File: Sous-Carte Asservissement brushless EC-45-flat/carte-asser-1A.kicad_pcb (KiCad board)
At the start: 2 copper layers, 60 x 62.5 mm, 57 parts, among them K1 Maxon-200142, K2 Maxon-200142, P1 swdio, P2 CAN bus, P3 usb, P4 serial bus, P5 5V, P6 8..24V, P7 encoder 1, P8 encoder 2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

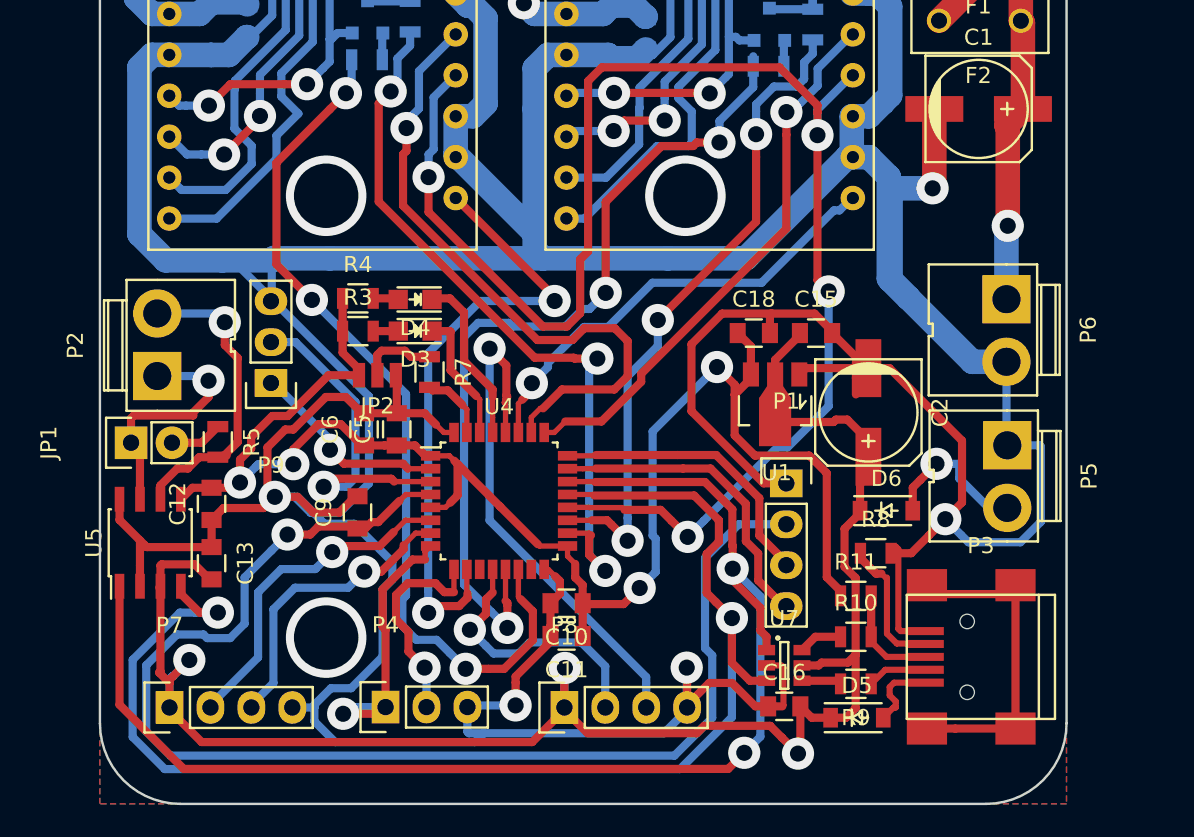
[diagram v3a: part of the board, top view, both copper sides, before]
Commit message: added B-plugs for power
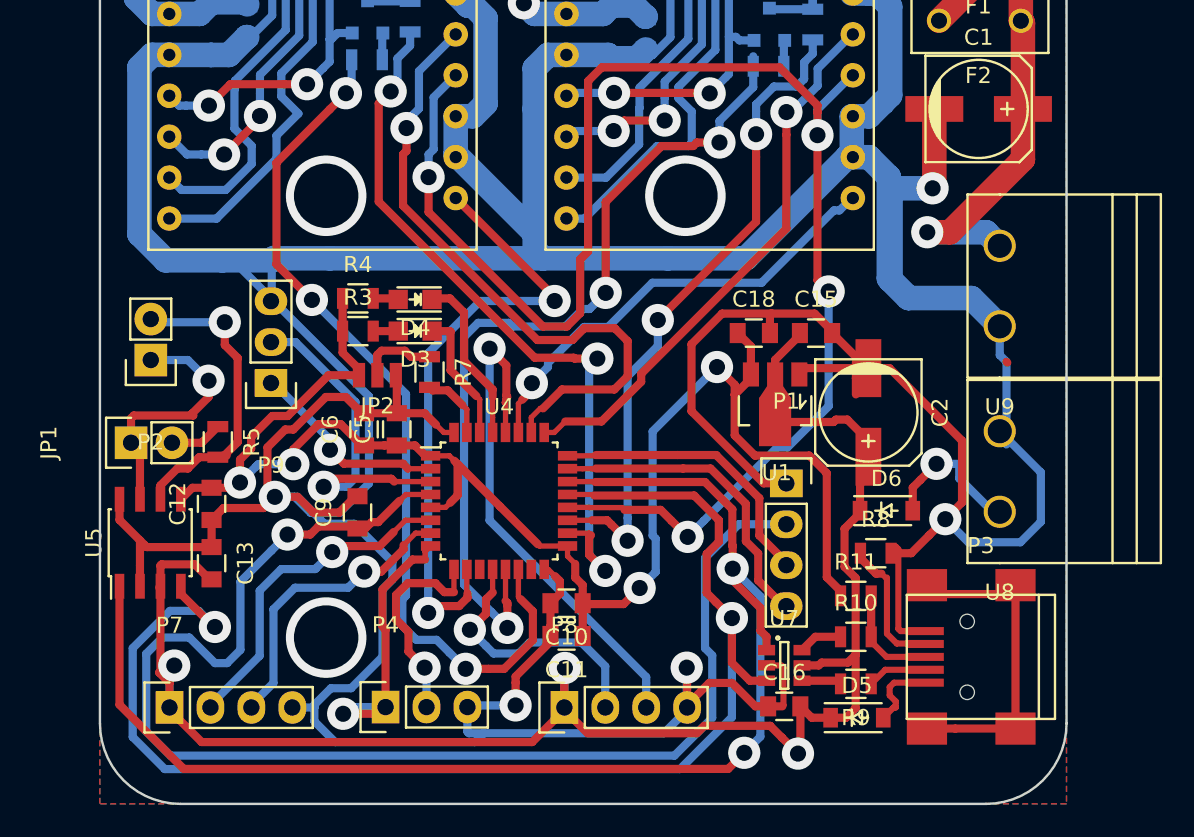
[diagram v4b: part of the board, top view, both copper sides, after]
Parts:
- removed P5: 5V, Connect:JWT_Vertical_A3963-RM3.96mm-2
- removed P6: 8..24V, Connect:JWT_Vertical_A3963-RM3.96mm-2
- added U8: 5v input, lib:B-plug-5mm, F.Cu at (169.3, 107.1)
- added U9: 12v input, lib:B-plug-5mm, F.Cu at (169.3, 95.6)
- P2: footprint Connect:JWT_Vertical_A3963-RM3.96mm-2 -> Pin_Headers:Pin_Header_Straight_1x02
- moved P2 1.07 mm to (116.6, 100.2), turned to 180 degrees
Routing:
- net +24V: track 22.8 -> 26.3 mm
- net /uC-part/nrst: track 81.3 -> 83.7 mm
- net +5V: track 109.4 -> 107.9 mm
- net Net-(JP1-Pad1): track 15.6 -> 16.9 mm
- net /uC-part/can_rx: track 82.5 -> 83.4 mm
- net GND: track 424.8 -> 425.5 mm
- net Net-(P2-Pad2): track 19.3 -> 20.0 mm

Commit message: added a nice logo :)
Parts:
- added G***: LOGO, logo:phelma-logo, B.Cu at (166.7, 68.9)
- added G***: LOGO, logo:phelma-logo-exp, B.Cu at (140.8, 108.2)
- moved F2 1.15 mm to (168.2, 78.0)
- moved F1 1.00 mm to (168.3, 73.9)
- moved P2 0.98 mm to (115.8, 99.7)
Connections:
- U4 pad 18: /uC-part/pwm2_pos -> /uC-part/pwm1_pos
- U4 pad 19: /uC-part/pwm1_pos -> /uC-part/pwm2_pos
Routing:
- net /uC-part/pwm1_pos: track 40.9 -> 53.1 mm
- net GND: track 425.5 -> 437.6 mm
- net /uC-part/pwm2_pos: track 46.9 -> 56.7 mm
- net Net-(D6-Pad2): track 9.82 -> 18.2 mm
- net /uC-part/gpio_direction2: track 40.2 -> 47.7 mm
- net /encoder-part/encoder2_2: track 32.1 -> 37.7 mm
- net Net-(JP1-Pad1): track 16.9 -> 12.0 mm, vias 1 -> 0
- net +3V3: track 100.2 -> 104.2 mm
- net Net-(P2-Pad2): track 20.0 -> 23.7 mm
- net /uC-part/gpio_direction1: track 34.5 -> 36.8 mm
- net /uC-part/pwm1_neg: track 53.4 -> 55.7 mm
- net /uC-part/gpio_enable: track 96.0 -> 94.1 mm
- net /uC-part/gpio_ready2: track 38.9 -> 40.2 mm
- net /uC-part/nrst: track 83.7 -> 84.9 mm
- net /brushless-part/power2: track 79.7 -> 78.5 mm
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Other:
- rule trace_min: 0.2 -> 0.007874
- rule via_min_size: 0.4 -> 0.015748
- board text added: "5v a b gnd"
- board text added: "5v gnd"
- board text added: "Logo : Antonin Macquart"
- board text added: "Lucien Dos Santos Farret RobotroniK Phelma 2016"
- board text added: "Motor A"
- board text added: "Motor B"
- board text added: "canl canh"
- board text added: "gnd 24v"
- board text added: "gnd scl sda"
- board text added: "rx tx gnd"

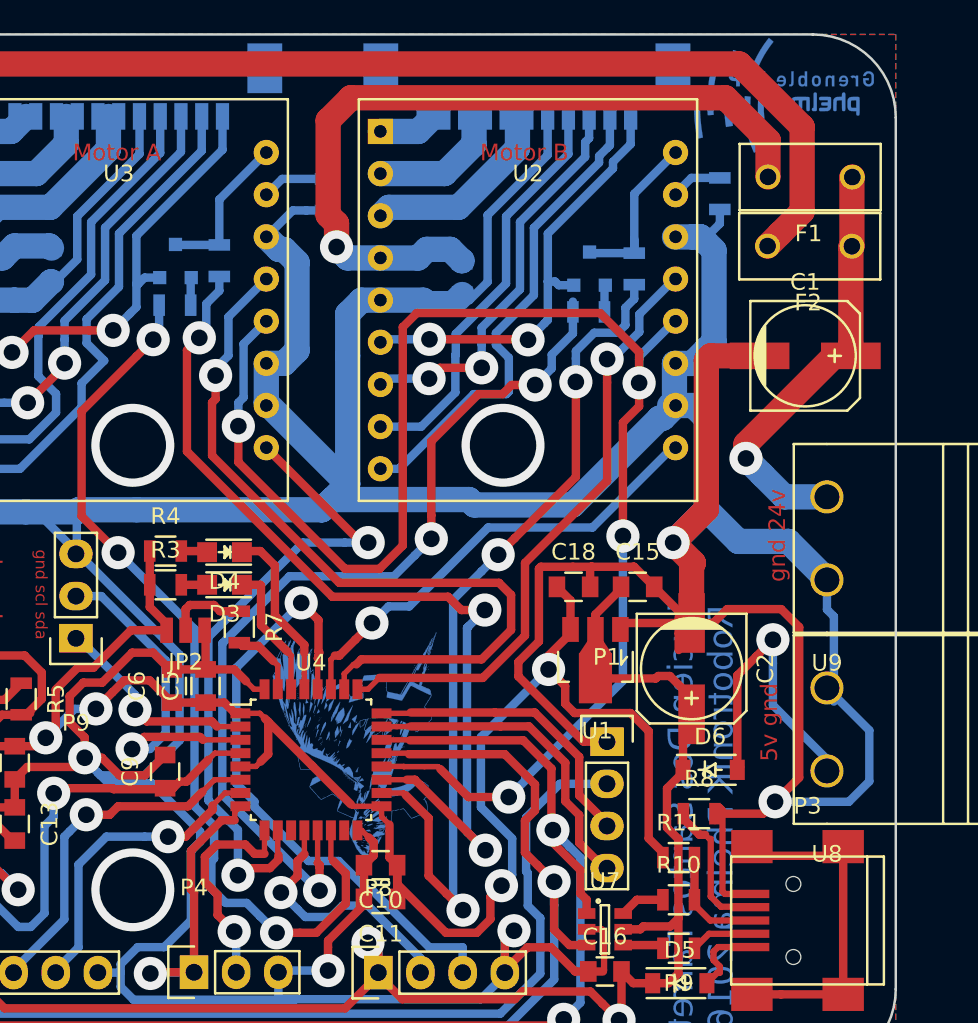
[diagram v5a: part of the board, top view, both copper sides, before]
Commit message: asser 1A : BOM + ready for pisa !
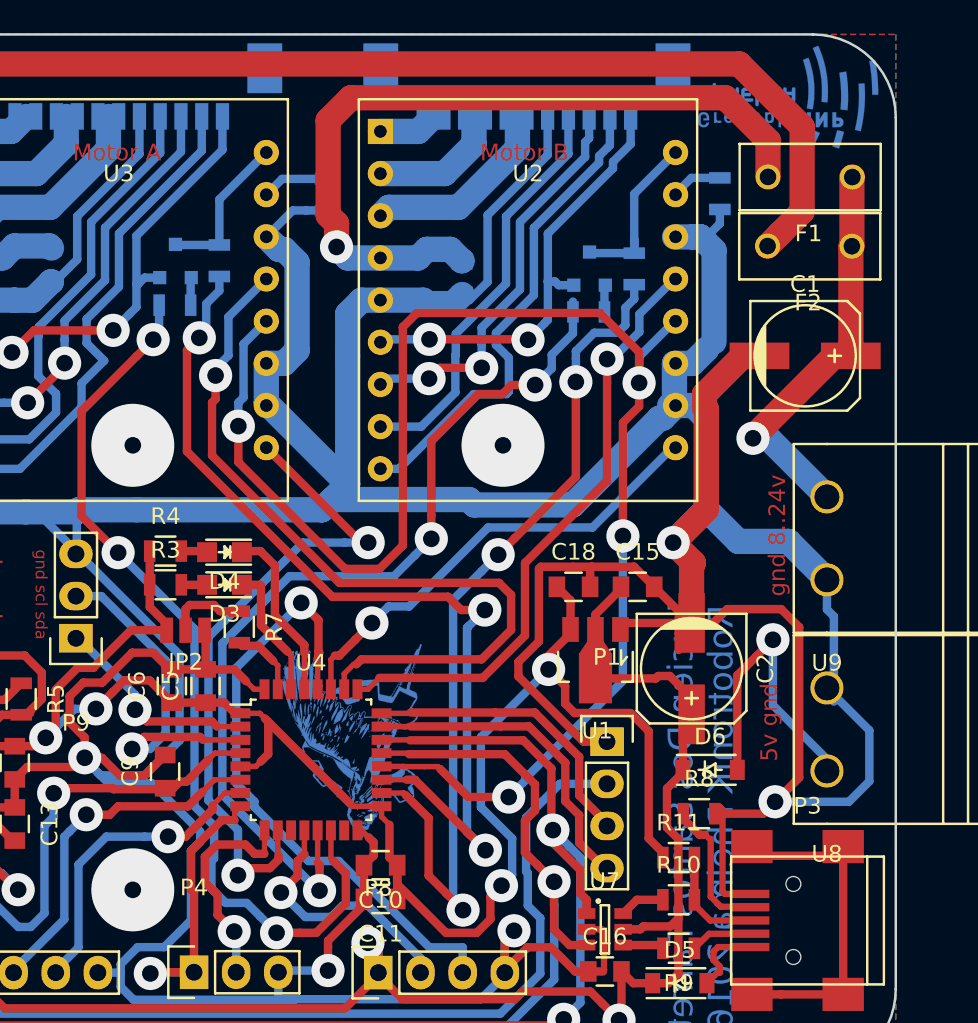
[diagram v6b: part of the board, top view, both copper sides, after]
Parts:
- removed the G*** at (140.8, 108.2)
- added G***: LOGO, logo:phelma-logo-exp3, B.Cu at (140.6, 107.9)
- C1: footprint Capacitors_SMD:c_elec_6.3x4.5 -> Capacitors_SMD:c_elec_6.3x7.7
- C2: footprint Capacitors_SMD:c_elec_6.3x4.5 -> Capacitors_SMD:c_elec_6.3x5.8
- moved G*** 0.59 mm to (166.9, 69.4), turned to 0 degrees
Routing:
- net GND: track 437.6 -> 434.9 mm
- net +24V: track 26.7 -> 25.4 mm
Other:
- board text added: "gnd 8..24v"
- board text removed: "gnd 24v"

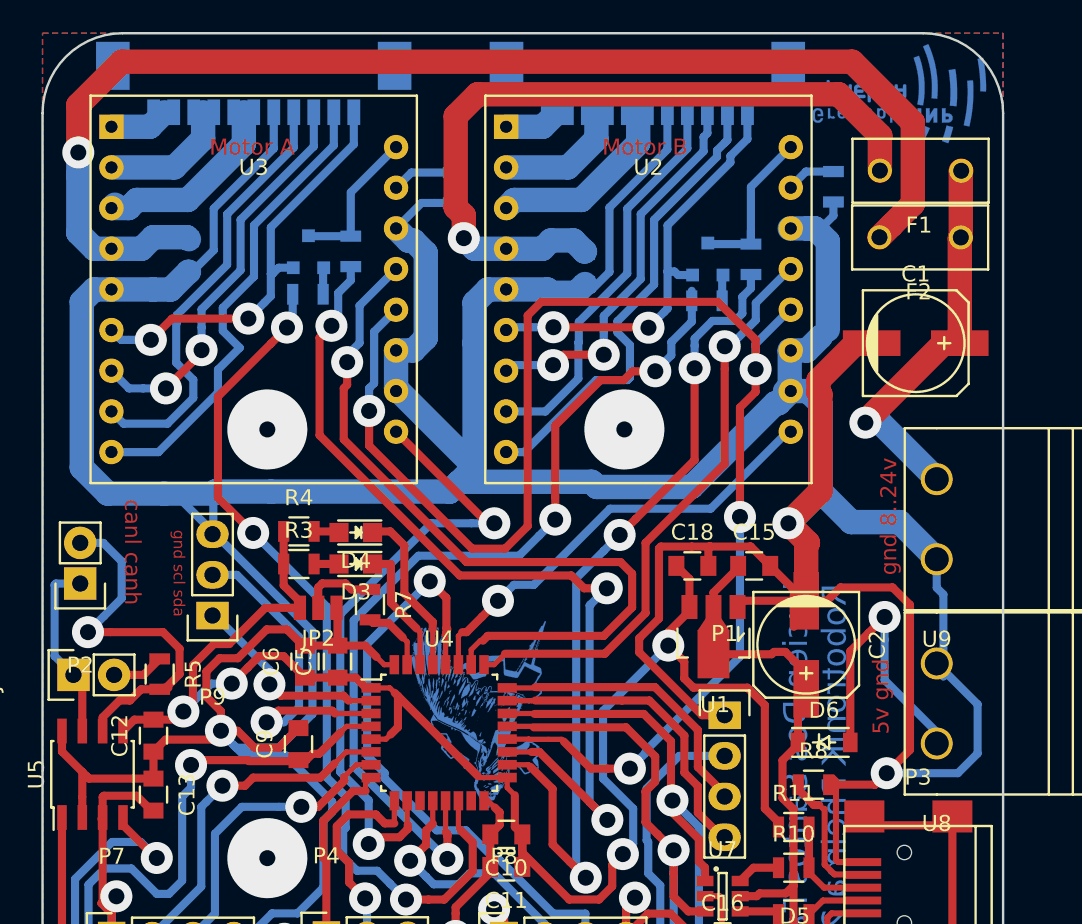
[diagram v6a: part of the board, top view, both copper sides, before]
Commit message: asser 1A : corrected zif sockets
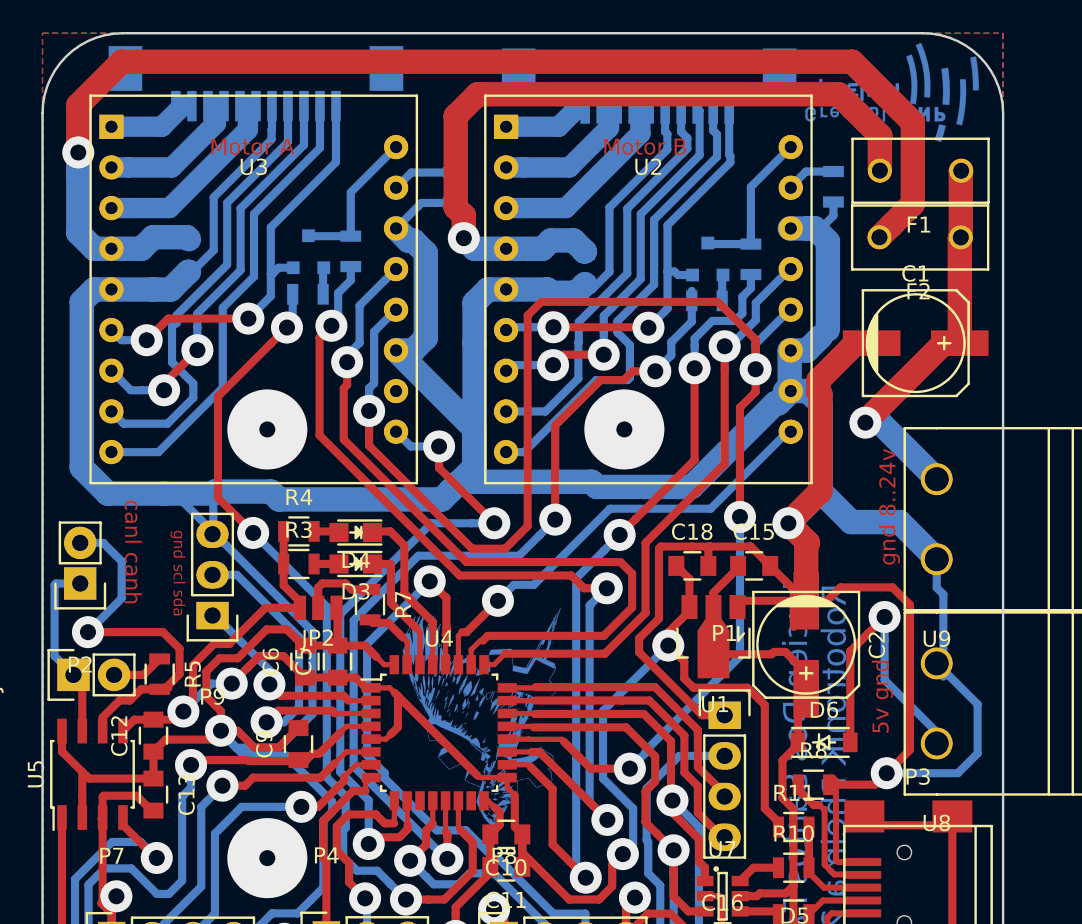
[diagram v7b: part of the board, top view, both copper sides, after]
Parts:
- removed the G*** at (140.6, 107.9)
- added G***: LOGO, logo:phelma-logo-exp, B.Cu at (140.8, 108.1)
- K1, K2: footprint Connectors_Molex:Molex_PicoBlade_53261-1171 -> de24-2:Molex-52207-0433
- moved K1 2.67 mm to (151.3, 70.0)
- moved K2 2.52 mm to (126.8, 69.8)
- moved G*** 0.46 mm to (166.5, 69.4)
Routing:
- net /uC-part/gpio_ready2: track 40.2 -> 41.4 mm, vias 2 -> 3
- net /brushless-part/W1_1: track 4.81 -> 5.90 mm
- net GND: track 434.9 -> 435.9 mm
- net /brushless-part/W2_1: track 4.94 -> 5.91 mm
- net Net-(K2-Pad10): track 29.6 -> 28.7 mm
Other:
- net class Default: clearance 0.3302 -> 0.254
- net class fat: clearance 0.508 -> 0.254; trace_width 1.524 -> 1.27
- rule trace_clearance: 0.3302 -> 0.254

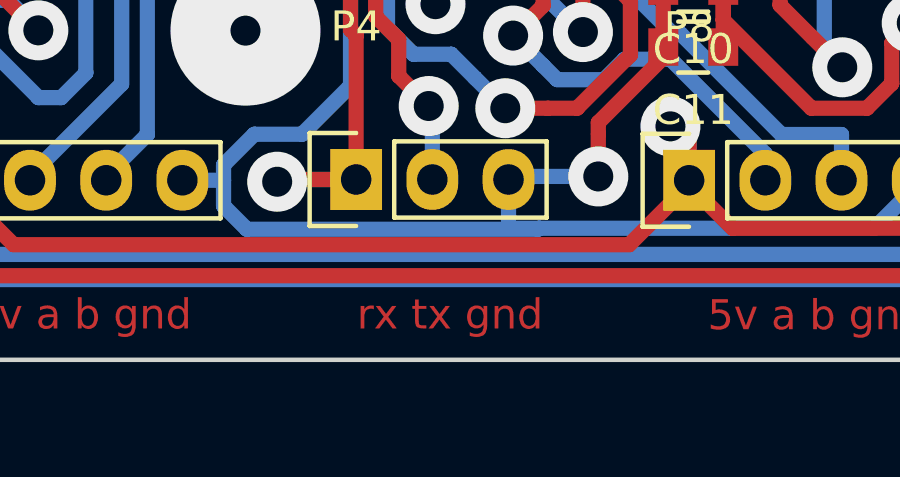
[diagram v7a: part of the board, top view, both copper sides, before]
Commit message: asser 1A : inversed serial tx and rx labels, damn
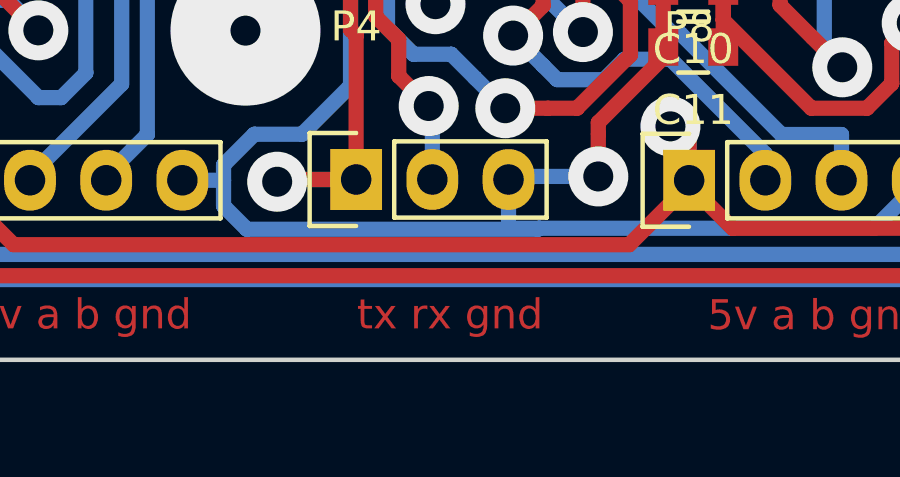
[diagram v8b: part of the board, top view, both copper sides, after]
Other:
- board text added: "tx rx gnd"
- board text removed: "rx tx gnd"
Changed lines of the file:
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@@
-(kicad_pcb (version 4) (host pcbnew 0.201604021231+6659~43~ubuntu15.10.1-product)
+(kicad_pcb (version 4) (host pcbnew 0.201604182031+6701~44~ubuntu15.10.1-product)
   (general
-    (links 0)
+    (links 156)
     (no_connects 0)
     (area 109.16894 60.025519 210.349326 135.523001)
@@
     (effects (font (size 1 1) (thickness 0.2)))
   )
-  (gr_text "rx tx gnd" (at 134.28444 126.26952) (layer F.Cu)
+  (gr_text "tx rx gnd" (at 134.28444 126.26952) (layer F.Cu)
     (effects (font (size 1 1) (thickness 0.2)))
   )
